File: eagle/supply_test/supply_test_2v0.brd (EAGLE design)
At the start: 94 x 50.8 mm, 47 parts, among them J1 SOCKET, J10 SOCKET, J11 SOCKET, J12 SOCKET, J13 SOCKET, J14 SOCKET, J15 SOCKET, J16 SOCKET, J17 SOCKET, J18 SOCKET, J19 SOCKET, J2 SOCKET, J20 SOCKET, J21 AC_INSW, J22 SOCKET, J23 MA02-1STR, J3 SOCKET, J4 SOCKET, J5 SOCKET, J6 SOCKET, J7 SOCKET, J8 SOCKET, J9 SOCKET

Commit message: supply test version 2
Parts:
- removed C4: (no value), rcl:C0603
- removed D4: ZENERBZT52, powerfilm:BZT52
- removed J23: MA02-1STR, con-lstb:MA02-1
- removed R7: 1k, rcl:R0603
- removed TP3: TP_STD, skyspecs:TP
- added U1: TPS62122, powerfilm:WDFN-6
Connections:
- removed net N$10: C4.1, D4.C, R7.2, TP3.P$1
- removed net N$9: J23.2, R7.1
- net GND: no longer C4.2, D4.A
- net VCC: no longer J23.1
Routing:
- net N$10: track 17.9 -> 0.00 mm
- net VCC: track 35.5 -> 31.7 mm
- net N$9: track 1.94 -> 0.00 mm
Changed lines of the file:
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@@
 <attribute name="NAME" x="70.866" y="24.892" size="1.27" layer="25"/>
-</element>
-<element name="R7" library="rcl" package="R0603" value="1k" x="81.026" y="40.64" smashed="yes" rot="R180">
-<attribute name="NAME" x="79.121" y="41.021" size="1.27" layer="25" rot="R180"/>
-<attribute name="DIGIKEY" value="P1.0KGCT-ND" x="81.026" y="40.64" size="1.778" layer="27" rot="R180" display="off"/>
-</element>
-<element name="D4" library="powerfilm" package="BZT52" value="ZENERBZT52" x="81.026" y="43.18" smashed="yes" rot="R180">
-<attribute name="DIGIKEY" value="BZT52C3V3T-7DICT-ND" x="81.026" y="43.18" size="1.778" layer="27" rot="R180" display="off"/>
-<attribute name="NAME" x="79.248" y="43.688" size="1.27" layer="25" rot="R180"/>
-</element>
-<element name="J23" library="con-lstb" package="MA02-1" value="MA02-1STR" x="85.09" y="40.64" smashed="yes" rot="R180">
-<attribute name="NAME" x="85.09" y="42.799" size="1.27" layer="25" ratio="10"/>
-<attribute name="DIGIKEY" value="609-4434-ND" x="85.09" y="40.64" size="1.778" layer="27" rot="R180" display="off"/>
-</element>
-<element name="C4" library="rcl" package="C0603" value="" x="81.28" y="44.45" smashed="yes">
-<attribute name="NAME" x="79.375" y="45.847" size="1.27" layer="25" rot="R180"/>
-<attribute name="VALUE" x="80.645" y="42.545" size="1.27" layer="27"/>
-<attribute name="DIGIKEY" value="445-8028-1-ND" x="81.28" y="44.45" size="1.778" layer="27" display="off"/>
-</element>
-<element name="TP3" library="skyspecs" package="TP" value="TP_STD" x="91.694" y="42.672" smashed="yes">
-<attribute name="DIGIKEY" value="5000K-ND " x="91.694" y="42.672" size="1.778" layer="27" display="off"/>
 </element>
 <element name="RV1" library="powerfilm" package="MOV_4032" value="275VAC" x="40.64" y="25.4" smashed="yes">
@@
 </element>
 <element name="U$1" library="umich" package="UMICH" value="" x="50.546" y="2.032"/>
+<element name="U1" library="powerfilm" package="WDFN-6" value="TPS62122" x="1.27" y="-3.81">
+<attribute name="DIGIKEY" value="296-27695-1-ND" x="1.27" y="-3.81" size="1.778" layer="27" display="off"/>
+</element>
 </elements>
 <signals>
@@
 <wire x1="63.5" y1="24.892" x2="77.724" y2="24.892" width="0.8128" layer="16"/>
 <wire x1="77.724" y1="24.892" x2="79.248" y2="23.368" width="0.8128" layer="16"/>
-<contactref element="D4" pad="A"/>
-<contactref element="C4" pad="2"/>
 <via x="84.328" y="44.45" extent="1-16" drill="0.6"/>
 <via x="84.328" y="43.18" extent="1-16" drill="0.6"/>
@@
 <wire x1="83.82" y1="24" x2="85.656" y2="24" width="0.8128" layer="1"/>
 <wire x1="85.656" y1="24" x2="86.36" y2="24.704" width="0.8128" layer="1"/>
+<wire x1="84.328" y1="43.18" x2="84.328" y2="44.45" width="0" layer="19" extent="1-1"/>
 </signal>
 <signal name="N$12">
@@
 <wire x1="91.398" y1="26.504" x2="91.694" y2="26.8" width="0.8128" layer="1"/>
 <wire x1="88.9" y1="29.464" x2="88.9" y2="26.504" width="0.8128" layer="1"/>
-<contactref element="J23" pad="1"/>
-<wire x1="86.36" y1="40.64" x2="86.36" y2="36.83" width="0.8128" layer="1"/>
 <wire x1="86.36" y1="36.83" x2="88.9" y2="34.29" width="0.8128" layer="1"/>
 <wire x1="88.9" y1="34.29" x2="88.9" y2="32.512" width="0.8128" layer="1"/>
@@
 <wire x1="63.23" y1="24.4" x2="65.278" y2="22.352" width="0.8128" layer="1"/>
 </signal>
-<signal name="N$9">
-<contactref element="R7" pad="1"/>
-<contactref element="J23" pad="2"/>
-<wire x1="81.876" y1="40.64" x2="83.82" y2="40.64" width="0.8128" layer="1"/>
-</signal>
-<signal name="N$10">
-<contactref element="R7" pad="2"/>
-<contactref element="D4" pad="C"/>
-<contactref element="TP3" pad="P$1"/>
-<contactref element="C4" pad="1"/>
-<wire x1="80.326" y1="43.18" x2="80.326" y2="44.346" width="0.8128" layer="1"/>
-<wire x1="80.326" y1="44.346" x2="80.43" y2="44.45" width="0.8128" layer="1"/>
-<wire x1="80.176" y1="40.64" x2="80.176" y2="43.03" width="0.8128" layer="1"/>
-<wire x1="80.176" y1="43.03" x2="80.326" y2="43.18" width="0.8128" layer="1"/>
-<wire x1="80.43" y1="44.45" x2="80.43" y2="45.632" width="0.4064" layer="1"/>
-<wire x1="80.43" y1="45.632" x2="80.772" y2="45.974" width="0.4064" layer="1"/>
-<wire x1="80.772" y1="45.974" x2="86.868" y2="45.974" width="0.4064" layer="1"/>
-<wire x1="86.868" y1="45.974" x2="90.17" y2="42.672" width="0.4064" layer="1"/>
-<wire x1="90.17" y1="42.672" x2="91.694" y2="42.672" width="0.4064" layer="1"/>
-</signal>
 <signal name="N$11">

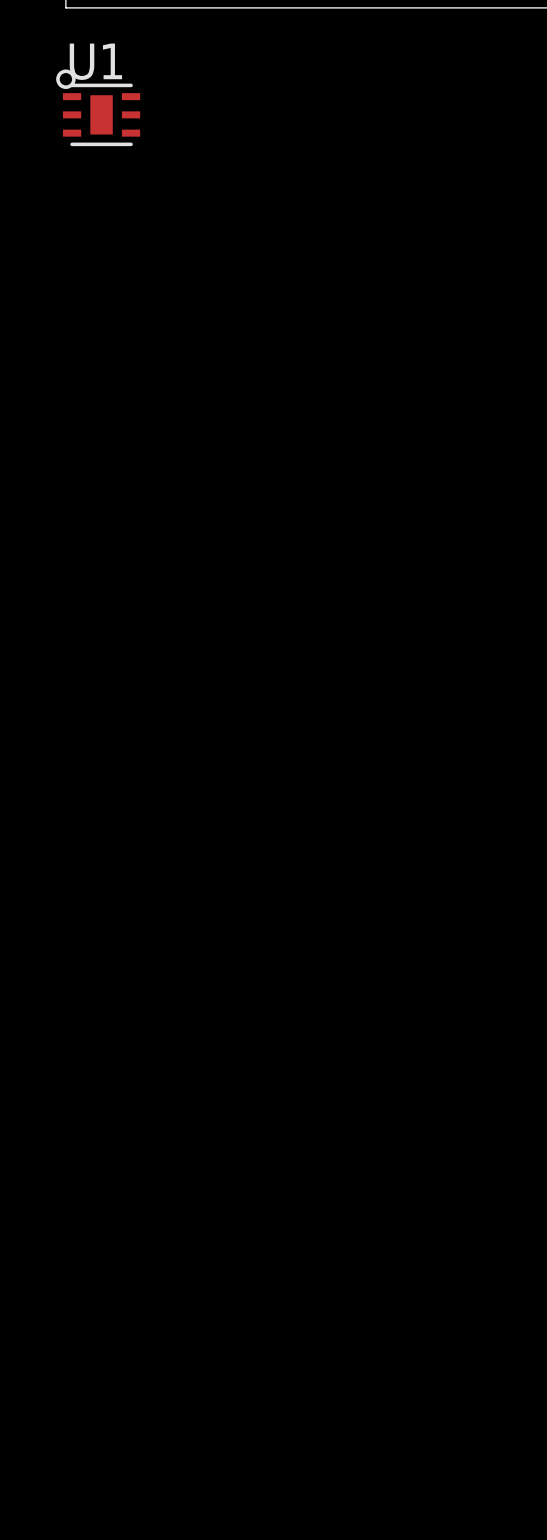
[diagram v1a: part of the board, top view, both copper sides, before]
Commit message: added different regulator to supply test
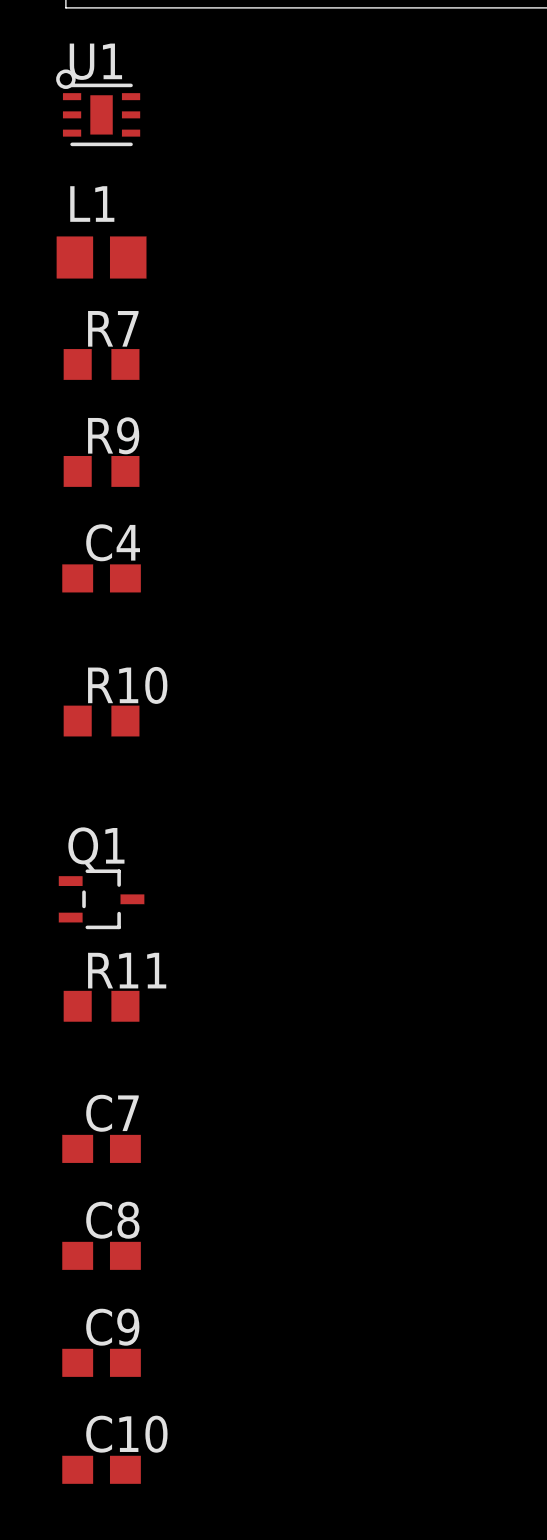
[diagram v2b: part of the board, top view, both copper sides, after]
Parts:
- added C10, C7: 4.7uF, rcl:C0603
- added C4: 22pF, rcl:C0603
- added C8, C9: 0.1uF, rcl:C0603
- added L1: 10uH, rcl:L0805
- added Q1: 2N7002, nav:SC-70-3
- added R10, R11: 4.99k, rcl:R0603
- added R7: 560k, rcl:R0603
- added R9: 180k, rcl:R0603
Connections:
- new net +3V3: C10.1, C4.1, C9.1, L1.1, R7.2, U1.P2
- new net N$13: C4.2, R7.1, R9.2, U1.P3
- new net N$16: Q1.P3, R10.1, U1.P4
- new net N$9: L1.2, U1.P1
- new net PS_!EN!: Q1.P1, R11.1
- net GND: now also C10.2, C7.2, C8.2, C9.2, Q1.P2, R11.2, R9.1, U1.P6, U1.PAD
- net VCC: now also C7.1, C8.1, R10.2, U1.P5
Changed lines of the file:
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@@
 <?xml version="1.0" encoding="utf-8"?>
 <!DOCTYPE eagle SYSTEM "eagle.dtd">
-<eagle version="6.5.0">
+<eagle version="6.3">
 <drawing>
 <settings>
@@
 <attribute name="DIGIKEY" value="296-27695-1-ND" x="1.27" y="-3.81" size="1.778" layer="27" display="off"/>
 </element>
+<element name="L1" library="rcl" package="L0805" value="10uH" x="1.27" y="-8.89">
+<attribute name="DIGIKEY" value="490-4990-1-ND" x="1.27" y="-8.89" size="1.778" layer="27" display="off"/>
+</element>
+<element name="R7" library="rcl" package="R0603" value="560k" x="1.27" y="-12.7"/>
+<element name="R9" library="rcl" package="R0603" value="180k" x="1.27" y="-16.51"/>
+<element name="C4" library="rcl" package="C0603" value="22pF" x="1.27" y="-20.32"/>
+<element name="R10" library="rcl" package="R0603" value="4.99k" x="1.27" y="-25.4"/>
+<element name="Q1" library="nav" package="SC-70-3" value="2N7002" x="1.27" y="-31.75">
+<attribute name="DIGIKEY" value="2N7002WCT-ND" x="1.27" y="-31.75" size="1.778" layer="27" display="off"/>
+</element>
+<element name="R11" library="rcl" package="R0603" value="4.99k" x="1.27" y="-35.56"/>
+<element name="C7" library="rcl" package="C0603" value="4.7uF" x="1.27" y="-40.64"/>
+<element name="C8" library="rcl" package="C0603" value="0.1uF" x="1.27" y="-44.45"/>
+<element name="C9" library="rcl" package="C0603" value="0.1uF" x="1.27" y="-48.26"/>
+<element name="C10" library="rcl" package="C0603" value="4.7uF" x="1.27" y="-52.07"/>
 </elements>
 <signals>
@@
 <wire x1="83.82" y1="24" x2="85.656" y2="24" width="0.8128" layer="1"/>
 <wire x1="85.656" y1="24" x2="86.36" y2="24.704" width="0.8128" layer="1"/>
+<contactref element="R9" pad="1"/>
+<contactref element="U1" pad="P6"/>
+<contactref element="U1" pad="PAD"/>
+<contactref element="Q1" pad="P2"/>
+<contactref element="R11" pad="2"/>
+<contactref element="C8" pad="2"/>
+<contactref element="C7" pad="2"/>
+<contactref element="C9" pad="2"/>
+<contactref element="C10" pad="2"/>
 <wire x1="84.328" y1="43.18" x2="84.328" y2="44.45" width="0" layer="19" extent="1-1"/>
+<wire x1="2.32" y1="-3.16" x2="57.912" y2="24.384" width="0" layer="19" extent="1-1"/>
+<wire x1="1.27" y1="-3.81" x2="2.32" y2="-3.16" width="0" layer="19" extent="1-1"/>
+<wire x1="0.42" y1="-16.51" x2="1.27" y2="-3.81" width="0" layer="19" extent="1-1"/>
+<wire x1="0.17" y1="-32.4" x2="0.42" y2="-16.51" width="0" layer="19" extent="1-1"/>
+<wire x1="2.12" y1="-35.56" x2="0.17" y2="-32.4" width="0" layer="19" extent="1-1"/>
+<wire x1="2.12" y1="-40.64" x2="2.12" y2="-35.56" width="0" layer="19" extent="1-1"/>
+<wire x1="2.12" y1="-44.45" x2="2.12" y2="-40.64" width="0" layer="19" extent="1-1"/>
+<wire x1="2.12" y1="-48.26" x2="2.12" y2="-44.45" width="0" layer="19" extent="1-1"/>
+<wire x1="2.12" y1="-52.07" x2="2.12" y2="-48.26" width="0" layer="19" extent="1-1"/>
 </signal>
 <signal name="N$12">
@@
 <wire x1="86.36" y1="26.604" x2="84.016" y2="26.604" width="0.8128" layer="1"/>
 <wire x1="84.016" y1="26.604" x2="83.82" y2="26.8" width="0.8128" layer="1"/>
+<contactref element="C8" pad="1"/>
+<contactref element="U1" pad="P5"/>
+<contactref element="R10" pad="2"/>
+<contactref element="C7" pad="1"/>
+<wire x1="2.32" y1="-3.81" x2="83.82" y2="26.8" width="0" layer="19" extent="1-1"/>
+<wire x1="2.12" y1="-25.4" x2="2.32" y2="-3.81" width="0" layer="19" extent="1-1"/>
+<wire x1="0.42" y1="-40.64" x2="2.12" y2="-25.4" width="0" layer="19" extent="1-1"/>
+<wire x1="0.42" y1="-44.45" x2="0.42" y2="-40.64" width="0" layer="19" extent="1-1"/>
 </signal>
 <signal name="N$6">
@@
 <wire x1="27.41" y1="45.72" x2="34.8996" y2="45.72" width="1.27" layer="1"/>
 </signal>
+<signal name="N$13">
+<contactref element="U1" pad="P3"/>
+<contactref element="R7" pad="1"/>
+<contactref element="R9" pad="2"/>
+<contactref element="C4" pad="2"/>
+<wire x1="2.12" y1="-16.51" x2="2.12" y2="-20.32" width="0" layer="19" extent="1-1"/>
+<wire x1="0.42" y1="-12.7" x2="2.12" y2="-16.51" width="0" layer="19" extent="1-1"/>
+<wire x1="0.22" y1="-4.46" x2="0.42" y2="-12.7" width="0" layer="19" extent="1-1"/>
+</signal>
+<signal name="N$16">
+<contactref element="R10" pad="1"/>
+<contactref element="U1" pad="P4"/>
+<contactref element="Q1" pad="P3"/>
+<wire x1="0.42" y1="-25.4" x2="2.37" y2="-31.75" width="0" layer="19" extent="1-1"/>
+<wire x1="2.32" y1="-4.46" x2="0.42" y2="-25.4" width="0" layer="19" extent="1-1"/>
+</signal>
+<signal name="PS_!EN!">
+<contactref element="R11" pad="1"/>
+<contactref element="Q1" pad="P1"/>
+<wire x1="0.17" y1="-31.1" x2="0.42" y2="-35.56" width="0" layer="19" extent="1-1"/>
+</signal>
+<signal name="N$9">
+<contactref element="U1" pad="P1"/>
+<contactref element="L1" pad="2"/>
+<wire x1="0.22" y1="-3.16" x2="2.22" y2="-8.89" width="0" layer="19" extent="1-1"/>
+</signal>
+<signal name="+3V3">
+<contactref element="U1" pad="P2"/>
+<contactref element="C4" pad="1"/>
+<contactref element="R7" pad="2"/>
+<contactref element="L1" pad="1"/>
+<contactref element="C10" pad="1"/>
+<contactref element="C9" pad="1"/>
+<wire x1="0.42" y1="-48.26" x2="0.42" y2="-52.07" width="0" layer="19" extent="1-1"/>
+<wire x1="0.42" y1="-20.32" x2="0.42" y2="-48.26" width="0" layer="19" extent="1-1"/>
+<wire x1="2.12" y1="-12.7" x2="0.42" y2="-20.32" width="0" layer="19" extent="1-1"/>
+<wire x1="0.32" y1="-8.89" x2="2.12" y2="-12.7" width="0" layer="19" extent="1-1"/>
+<wire x1="0.22" y1="-3.81" x2="0.32" y2="-8.89" width="0" layer="19" extent="1-1"/>
+</signal>
 </signals>

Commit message: miniaturized power supply
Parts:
- removed C2: (no value), rcl:C0805
- removed C5: (no value), SparkFun-Passives:EIA3216
- removed C6: (no value), rcl:C1210
- removed F1: 80mA FAST, powerfilm:FUSE
- removed J1, J10, J11, J12, J13, J14, J15, J16, J17, J18, J19, J2, J20, J22, J3, J4, J5, J6, J7, J8, J9: SOCKET, powerfilm:SOCKET_1MM
- removed RV1: 275VAC, powerfilm:MOV_4032
- R4, R5, R6: value 0 -> NP
- moved R2 122.5 mm to (1.27, -57.1)
- moved R3 118.2 mm to (1.27, -61.0)
- moved R4 115.1 mm to (1.27, -66.0)
- moved R5 114.2 mm to (1.27, -71.1)
- moved R6 113.3 mm to (1.27, -76.2)
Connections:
- removed net N$11: F1.M1A, F1.M1B, J21.L
- removed net N$12: J16.P1, J17.P1, R3.1, R4.2
- removed net N$14: F1.M2A, F1.M2B, J20.P1, R5.1, RV1.P2
- removed net N$15: J18.P1, J19.P1, R4.1, R5.2
- net GND: no longer C2.2, C5.C, C6.2, J10.P1, J12.P1
- net N$1: no longer J2.P1, J3.P1
- net N$2: no longer J1.P1, RV1.P1
- net N$3: now also D1.A, D2.C, R2.2; no longer C1.1, J4.P1, J5.P1, R6.1, R8.2
- net N$4: now also C1.1, R2.1, R4.1, R8.2; no longer D1.A, D2.C, J6.P1, J9.P1, R6.2
- net N$5: now also D3.P4, R4.2; no longer D1.C, J15.P1, J7.P1, R2.1, R3.2
- net N$6: now also J21.L, R3.1, R6.1; no longer D3.P2, J13.P1
- net N$7: now also R5.1; no longer J22.P1
- net N$8: now also D3.P2, R6.2; no longer D3.P4, J14.P1
- net VCC: now also D1.C, R3.2, R5.2; no longer C2.1, C5.A, C6.1, J11.P1, J8.P1, R2.2
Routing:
- net GND: track 84.5 -> 8.86 mm, vias 4 -> 1
- net N$14: track 39.2 -> 0.00 mm
- net N$11: track 26.9 -> 0.00 mm
- net N$5: track 21.5 -> 0.00 mm
- net N$12: track 17.3 -> 0.00 mm
- net N$2: track 33.2 -> 16.3 mm
- net N$15: track 16.6 -> 0.00 mm
- net VCC: track 31.7 -> 17.4 mm
- net N$7: track 11.9 -> 0.00 mm
- net N$4: track 22.9 -> 12.0 mm
- net N$1: track 22.0 -> 11.6 mm
- net N$3: track 22.9 -> 14.6 mm
- net N$6: track 6.38 -> 0.00 mm
- net N$8: track 4.17 -> 0.00 mm
